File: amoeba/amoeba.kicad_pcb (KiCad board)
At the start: 2 copper layers, 18.8 x 16.3 mm, 34 parts

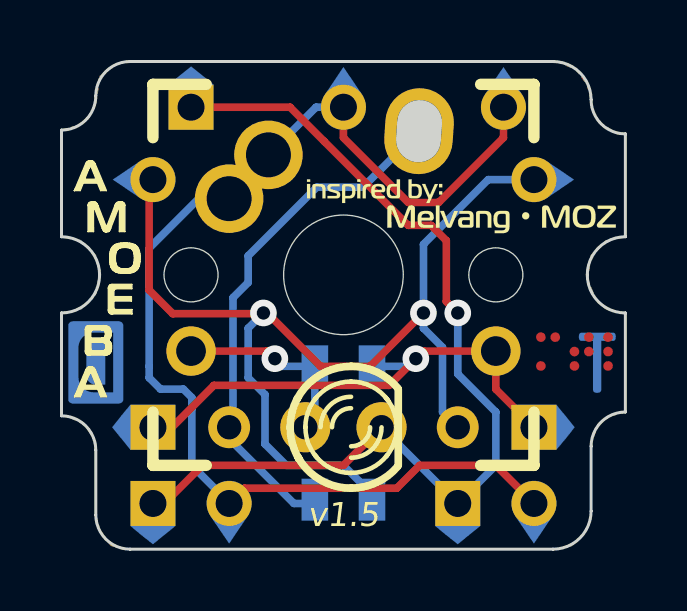
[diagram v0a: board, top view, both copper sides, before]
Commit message: added amoeba 1.6 w/choc footprint
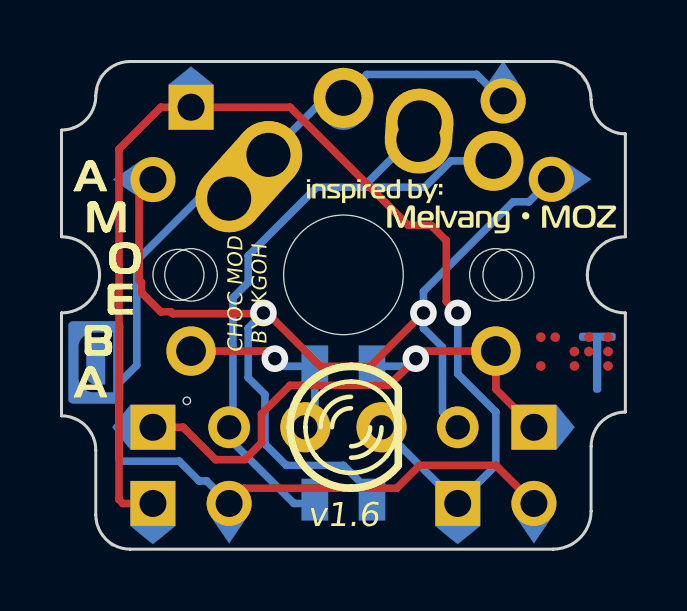
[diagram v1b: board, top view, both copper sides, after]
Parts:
- removed SC0:0: CONN_1, Pad
- S0: footprint ALPS_CHERRY_ZEAL_PCB_100H -> Keebio-Parts:MX-Alps-Choc-1U-NoLED
- moved pad-arrow-round 0.58 mm to (256.1, 107.3)
- moved SR0:1 0.58 mm to (256.5, 107.7)
- moved SC0:1 0.21 mm to (254.2, 104.7)
- moved pad-arrow-round 0.21 mm to (254.2, 104.4)
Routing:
- net /key/LC0: track 32.6 -> 39.8 mm
- net /key/switch/N-SD0: track 17.6 -> 22.4 mm
- net /key/LR0: track 17.1 -> 19.2 mm
- net /key/SC0: track 37.5 -> 36.1 mm
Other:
- outline, holes or cut-outs redrawn
- board text added: "CHOC MOD BY KGOH"
- board text added: "v1.6"
- board text removed: "v1.5"
